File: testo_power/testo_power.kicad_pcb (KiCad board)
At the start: 2 copper layers, 20 x 30 mm, 18 parts, among them J1 Conn_01x02_Socket, J2 Conn_01x02_Socket, J3 USB_C_Receptacle_PowerOnly_6P, Q1 IRLML6402TRPBF, U1 MCP73812

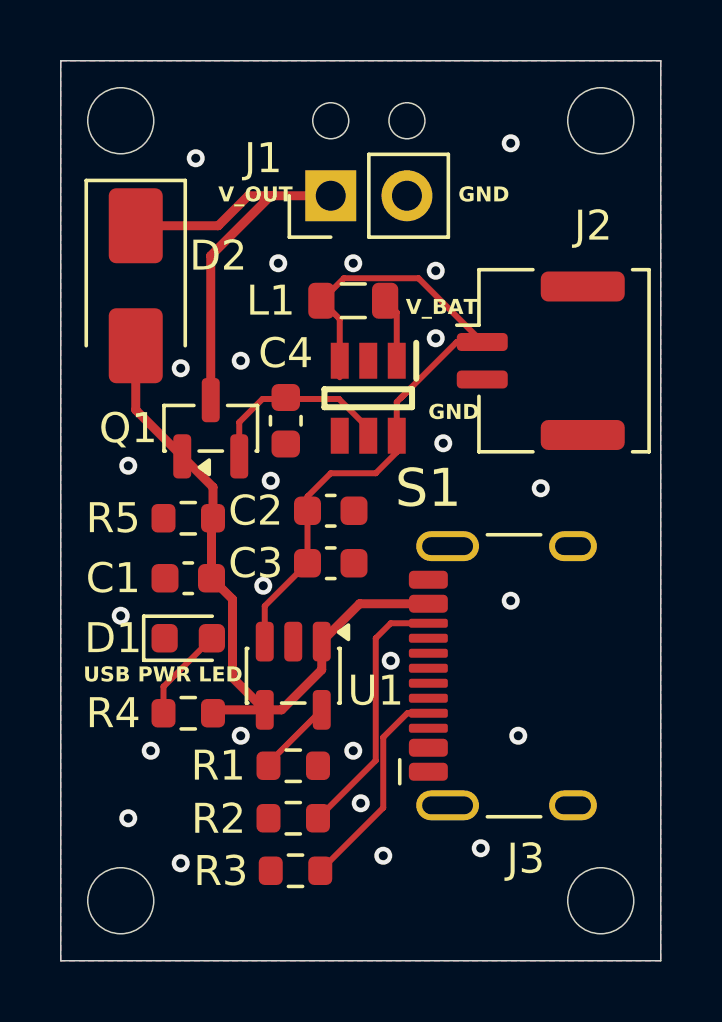
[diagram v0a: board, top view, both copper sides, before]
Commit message: changed position of c2 c3
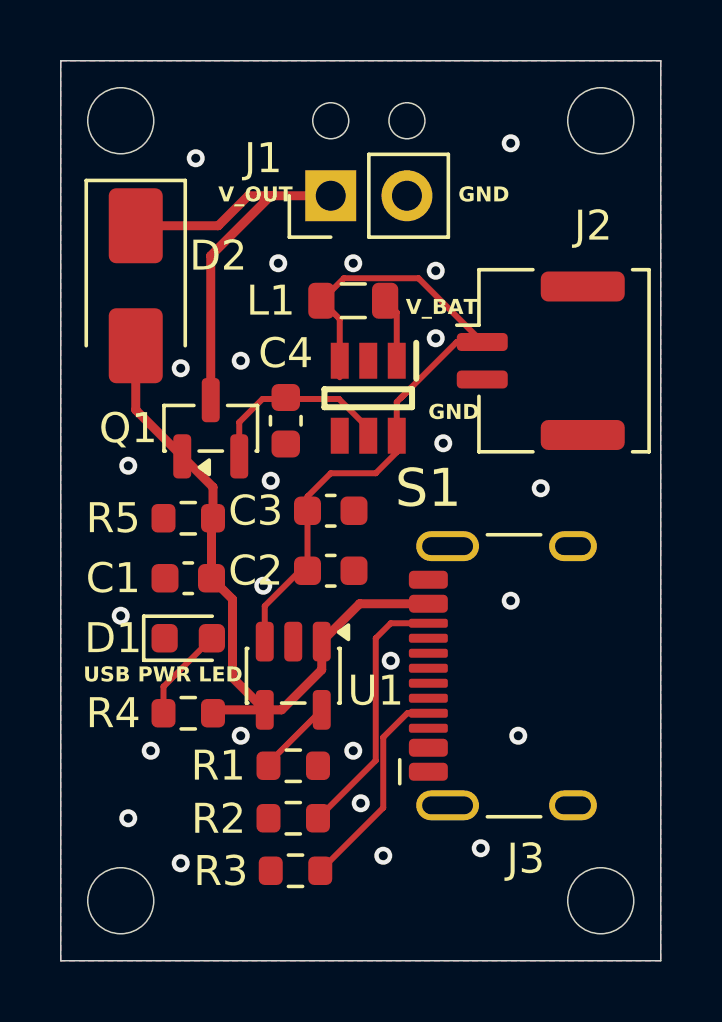
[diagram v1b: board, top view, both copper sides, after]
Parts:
- moved C2 2.00 mm to (109.0, 117.0)
- moved C3 1.75 mm to (109.0, 115.0)
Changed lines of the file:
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@@
 	(footprint "Capacitor_SMD:C_0603_1608Metric"
 		(layer "F.Cu")
-		(at 109 116.75)
+		(at 109 115)
 		(descr "Capacitor SMD 0603 (1608 Metric), square (rectangular) end terminal, IPC-7351 nominal, (Body size source: IPC-SM-782 page 76, https://www.pcb-3d.com/wordpress/wp-content/uploads/ipc-sm-782a_amendment_1_and_2.pdf)")
 		(tags "capacitor")
@@
 	(footprint "Capacitor_SMD:C_0603_1608Metric"
 		(layer "F.Cu")
-		(at 109 115)
+		(at 109 117)
 		(descr "Capacitor SMD 0603 (1608 Metric), square (rectangular) end terminal, IPC-7351 nominal, (Body size source: IPC-SM-782 page 76, https://www.pcb-3d.com/wordpress/wp-content/uploads/ipc-sm-782a_amendment_1_and_2.pdf)")
 		(tags "capacitor")
@@
 	)
 	(segment
+		(start 111 118.75)
+		(end 110.5 119.25)
+		(width 0.2)
+		(layer "F.Cu")
+		(net "Net-(J3-CC2)")
+	)
+	(segment
+		(start 110.5 123.325)
+		(end 108.575 125.25)
+		(width 0.2)
+		(layer "F.Cu")
+		(net "Net-(J3-CC2)")
+	)
+	(segment
+		(start 110.5 119.25)
+		(end 110.5 123.325)
+		(width 0.2)
+		(layer "F.Cu")
+		(net "Net-(J3-CC2)")
+	)
+	(segment
+		(start 112.255 118.75)
+		(end 111 118.75)
+		(width 0.2)
+		(layer "F.Cu")
+		(net "Net-(J3-CC2)")
+	)
+	(segment
 		(start 108.699999 120.300001)
 		(end 107.3625 121.6375)
@@
 	)
 	(segment
+		(start 106.925 123.412499)
+		(end 106.925 123.5)
+		(width 0.2)
+		(layer "F.Cu")
+		(net "Net-(U1-PROG)")
+	)
+	(segment
+		(start 108.699999 121.6375)
+		(end 106.925 123.412499)
+		(width 0.2)
+		(layer "F.Cu")
+		(net "Net-(U1-PROG)")
+	)
+	(segment
+		(start 108.65 127)
+		(end 110.75 124.9)
+		(width 0.2)
+		(layer "F.Cu")
+		(net "Net-(J3-CC1)")
+	)
+	(segment
+		(start 110.75 124.9)
+		(end 110.75 122.552501)
+		(width 0.2)
+		(layer "F.Cu")
+		(net "Net-(J3-CC1)")
+	)
+	(segment
+		(start 110.75 122.552501)
+		(end 111.552501 121.75)
+		(width 0.2)
+		(layer "F.Cu")
+		(net "Net-(J3-CC1)")
+	)
+	(segment
+		(start 111.552501 121.75)
+		(end 112.255 121.75)
+		(width 0.2)
+		(layer "F.Cu")
+		(net "Net-(J3-CC1)")
+	)
+	(segment
 		(start 105.95 113.1875)
 		(end 105.95 112.05)
@@
 	)
 	(segment
-		(start 108.65 127)
-		(end 110.75 124.9)
-		(width 0.2)
-		(layer "F.Cu")
-		(net "Net-(J3-CC1)")
-	)
-	(segment
-		(start 110.75 124.9)
-		(end 110.75 122.552501)
-		(width 0.2)
-		(layer "F.Cu")
-		(net "Net-(J3-CC1)")
-	)
-	(segment
-		(start 110.75 122.552501)
-		(end 111.552501 121.75)
-		(width 0.2)
-		(layer "F.Cu")
-		(net "Net-(J3-CC1)")
-	)
-	(segment
-		(start 111.552501 121.75)
-		(end 112.255 121.75)
-		(width 0.2)
-		(layer "F.Cu")
-		(net "Net-(J3-CC1)")
-	)
-	(segment
-		(start 111 118.75)
-		(end 110.5 119.25)
-		(width 0.2)
-		(layer "F.Cu")
-		(net "Net-(J3-CC2)")
-	)
-	(segment
-		(start 110.5 123.325)
-		(end 108.575 125.25)
-		(width 0.2)
-		(layer "F.Cu")
-		(net "Net-(J3-CC2)")
-	)
-	(segment
-		(start 110.5 119.25)
-		(end 110.5 123.325)
-		(width 0.2)
-		(layer "F.Cu")
-		(net "Net-(J3-CC2)")
-	)
-	(segment
-		(start 112.255 118.75)
-		(end 111 118.75)
-		(width 0.2)
-		(layer "F.Cu")
-		(net "Net-(J3-CC2)")
-	)
-	(segment
 		(start 111.2 108.3875)
 		(end 110.8125 108)
@@
 		(net "Net-(S1-SW)")
 	)
-	(segment
-		(start 106.925 123.412499)
-		(end 106.925 123.5)
-		(width 0.2)
-		(layer "F.Cu")
-		(net "Net-(U1-PROG)")
-	)
-	(segment
-		(start 108.699999 121.6375)
-		(end 106.925 123.412499)
-		(width 0.2)
-		(layer "F.Cu")
-		(net "Net-(U1-PROG)")
-	)
 	(zone

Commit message: Replace molex connector
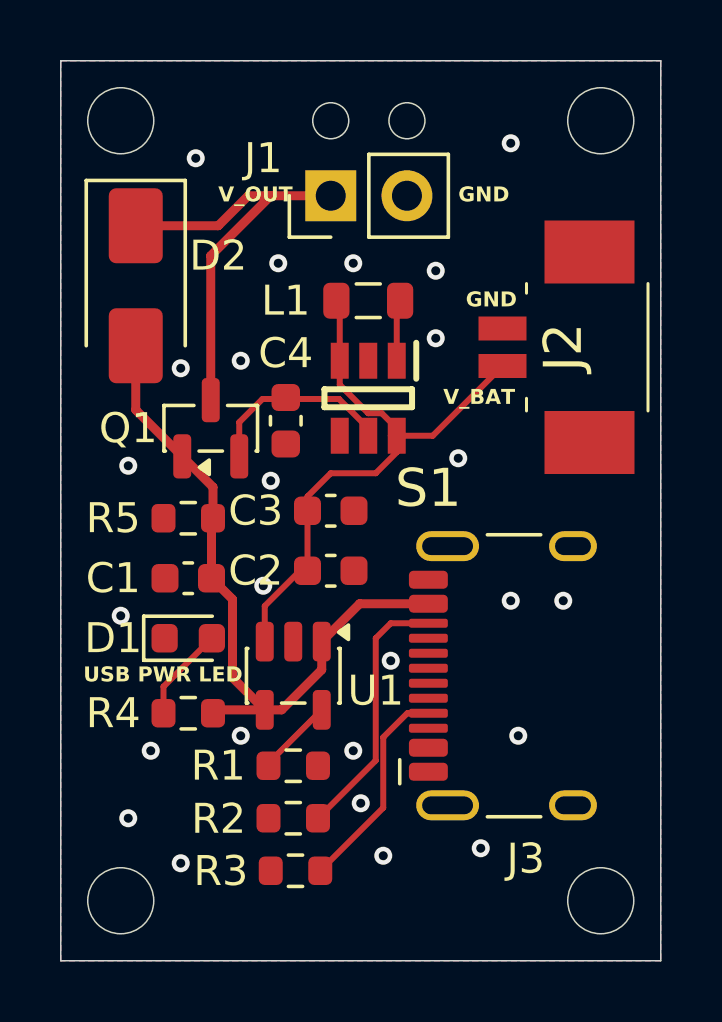
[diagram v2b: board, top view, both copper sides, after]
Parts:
- J2: footprint Connector_Molex:Molex_CLIK-Mate_502382-0270_1x02-1MP_P1.25mm_Vertical -> SamacSys_Parts:0532610271
- moved J2 0.89 mm to (115.5, 109.2), turned to 90 degrees
- moved L1 0.50 mm to (110.2, 108.0)
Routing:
- net BOOST_IN: track 24.2 -> 19.8 mm
